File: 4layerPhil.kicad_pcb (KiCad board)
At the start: 4 copper layers, 71 x 54 mm, 55 parts, among them J1 USB_C_Receptacle_USB2.0_16P, J2 Conn_01x05_Pin, J3 Conn_01x04_Pin, J6 1140084168, SW1 SW_SPDT, SW2 BTN1, SW3 BTN2, SW4 BTN3, U2 USBLC6-2SC6, U3 STM32F103RCTx, U4 SPX3819M5-L-3-3, Y1 16MHz

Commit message: Added colours to schematic
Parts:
- removed H1, H2, H3, H4: MountingHole, MountingHole:MountingHole_2.2mm_M2
- added FID1: Fiducial, Fiducial:Fiducial_1mm_Mask2mm, F.Cu at (116.5, 58.0)
- added FID2: Fiducial, Fiducial:Fiducial_1mm_Mask2mm, F.Cu at (116.2, 104.0)
- added FID3: Fiducial, Fiducial:Fiducial_1mm_Mask2mm, F.Cu at (169.0, 103.8)
- added MH1: M3, MountingHole:MountingHole_3.2mm_M3_Pad_Via, F.Cu at (111.1, 58.0)
- added MH2: M3, MountingHole:MountingHole_3.2mm_M3_Pad_Via, F.Cu at (174.0, 57.9)
- added MH3: M3, MountingHole:MountingHole_3.2mm_M3_Pad_Via, F.Cu at (111.0, 104.0)
- added MH4: M3, MountingHole:MountingHole_3.2mm_M3_Pad_Via, F.Cu at (174.0, 104.0)
- C1, C20, C22: footprint Capacitor_SMD:C_0603_1608Metric -> Capacitor_SMD:C_0805_2012Metric
- moved U4 41.0 mm to (160.1, 79.8), turned to 180 degrees
- moved R8 40.4 mm to (170.5, 65.8), turned to 180 degrees
- moved C21 38.8 mm to (160.0, 77.2)
- moved R24 38.2 mm to (167.3, 74.2), turned to 180 degrees
- moved C22 36.5 mm to (157.0, 79.7), turned to 90 degrees
- moved C20 33.9 mm to (163.2, 79.8), turned to -90 degrees
- moved C19 31.0 mm to (166.6, 76.5), turned to -90 degrees
- moved R7 29.1 mm to (172.0, 78.0), turned to 180 degrees
- moved C18 28.8 mm to (168.1, 76.5), turned to -90 degrees
- moved U2 6.94 mm to (165.4, 71.8)
- moved R4 3.72 mm to (153.2, 73.6)
- moved R2 3.72 mm to (153.2, 77.6)
- moved R3 3.72 mm to (153.2, 75.6)
- moved D2 3.04 mm to (148.2, 77.8)
- moved D3 3.04 mm to (148.2, 75.6)
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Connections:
- net Net-(U4-BP) renamed /BP_REG
- U2 pad 1: /USB_D- -> /USB_D+
- U2 pad 3: /USB_D+ -> /USB_D-
- U2 pad 4: /D_USB+ -> /D_USB-
- U2 pad 6: /D_USB- -> /D_USB+
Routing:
- net +3V3: track 218.9 -> 180.5 mm, vias 21 -> 18
- net VBUSF: track 0.00 -> 10.7 mm
- net /USR_LED_RED: track 8.32 -> 0.00 mm
- net /USBCC1: track 0.00 -> 7.64 mm
- net /USR_LED_BLU: track 7.60 -> 0.00 mm
- net /USBCC2: track 0.00 -> 7.54 mm
- net /USB_D-: track 13.8 -> 20.9 mm
- net /USB_D+: track 13.8 -> 20.9 mm
- net VBUS: track 0.00 -> 7.01 mm, vias 0 -> 1
- net /USR_LED_GRN: track 6.87 -> 0.00 mm
- net GND: track 62.8 -> 56.2 mm, vias 27 -> 34
- net /D_USB+: track 2.25 -> 8.37 mm
- net /D_USB-: track 2.24 -> 7.34 mm
- net /USR_LED_GRN_K: track 4.43 -> 0.00 mm
- net /USR_LED_BLU_K: track 4.33 -> 0.00 mm
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- added copper zone on B.Cu, net GND
- removed copper zone on In1.Cu, net GND
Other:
- outline, holes or cut-outs redrawn
- copper layers 4 -> 2

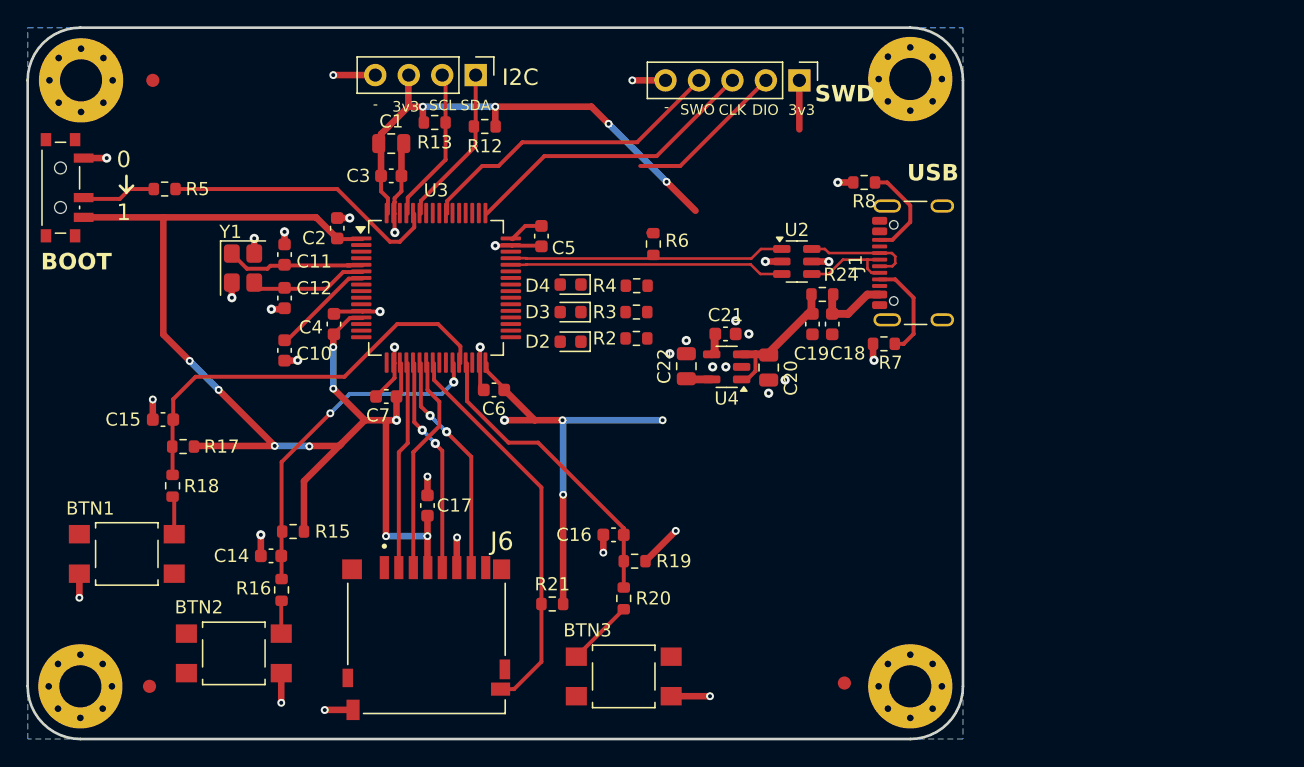
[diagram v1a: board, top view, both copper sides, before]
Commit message: New microSD card
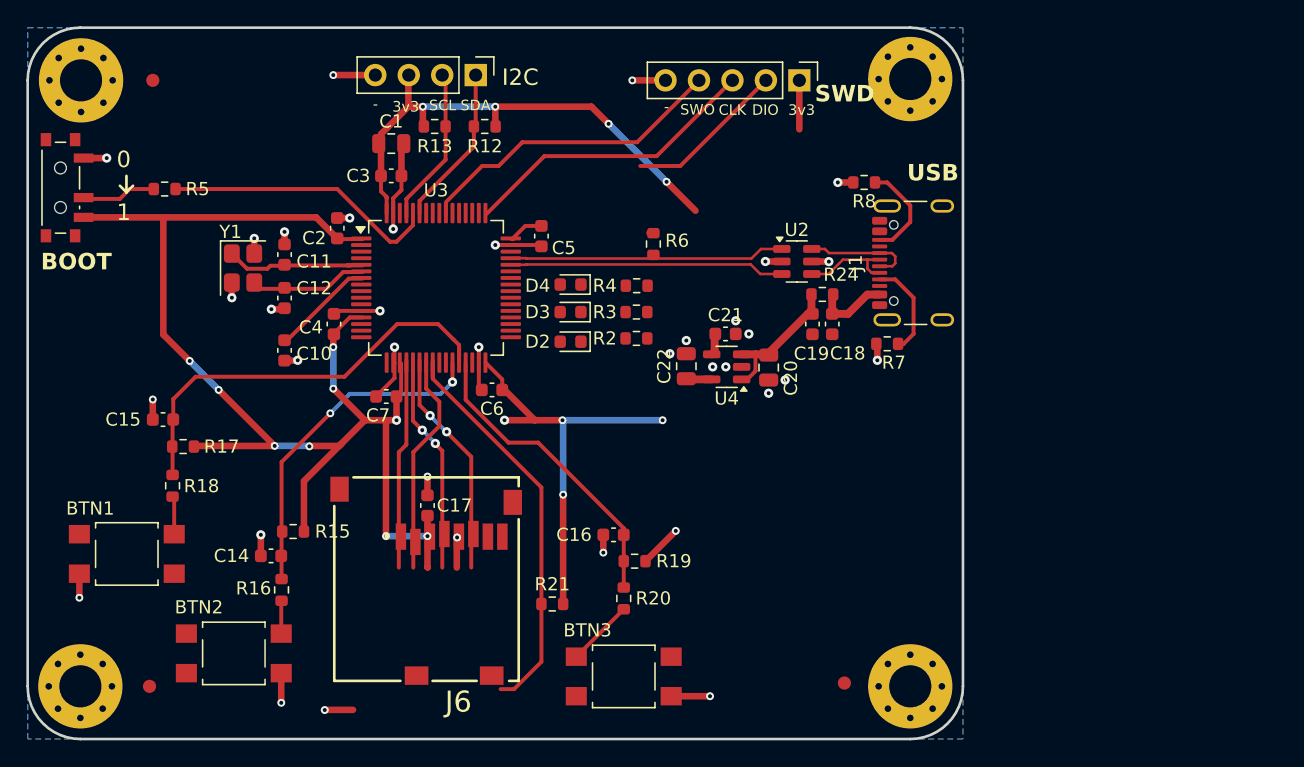
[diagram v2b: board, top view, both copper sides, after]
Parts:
- J6: footprint MicroSD_Socket:AMPHENOL_1140084168 -> MicroSD_Socket:GCT_MEM2061-01-188-00-A_REVA
- moved R13 0.30 mm to (137.9, 61.5)
- moved R7 0.25 mm to (172.2, 78.0)
- moved C6 0.15 mm to (142.2, 81.5)
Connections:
- net /USR_LED_BLU_K renamed /LED_BLU_K
- net /USR_LED_GRN renamed /LED_GRN
- net /USR_LED_GRN_K renamed /LED_GRN_K
- net /USR_LED_RED_K renamed /LED_RED_K
- net VBUS renamed +VBUS
- net VBUSF renamed +VBUSF
- D2 pad 2: /USR_LED_RED -> /LED_BLU
- D3 pad 2: /USR_LED_BLU -> /LED_BLU
- J1 pad A6: /D_USB+ -> /USB_D+
- J1 pad A7: /D_USB- -> /USB_D-
- J1 pad B6: /D_USB+ -> /USB_D+
- J1 pad B7: /D_USB- -> /USB_D-
- R6 pad 2: /USB_D+ -> /USB_D_ESD+
- U2 pad 1: /USB_D+ -> /USB_D_ESD+
- U2 pad 3: /USB_D- -> /USB_D_ESD-
- U2 pad 4: /D_USB- -> /USB_D-
- U2 pad 6: /D_USB+ -> /USB_D+
- U3 pad 40: /USR_LED_RED -> /LED_BLU
- U3 pad 41: /USR_LED_BLU -> /LED_BLU
- U3 pad 44: /USB_D- -> /USB_D_ESD-
- U3 pad 45: /USB_D+ -> /USB_D_ESD+
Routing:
- net /USB_D_ESD+: track 0.00 -> 20.9 mm
- net /USB_D_ESD-: track 0.00 -> 20.9 mm
- net /USB_D-: track 20.9 -> 7.34 mm
- net /USB_D+: track 20.9 -> 8.37 mm
- net /D_USB+: track 8.37 -> 0.00 mm
- net /D_USB-: track 7.34 -> 0.00 mm
- net SPI_SCK: track 16.4 -> 19.0 mm, vias 2 -> 3
- net GND: track 56.2 -> 53.6 mm, vias 34 -> 33
- net MICROSD_DETB: track 30.0 -> 31.4 mm
- net USR_BTN_2: track 31.9 -> 33.1 mm

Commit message: Managed to make the PCB ~5 mm smaller in both directions
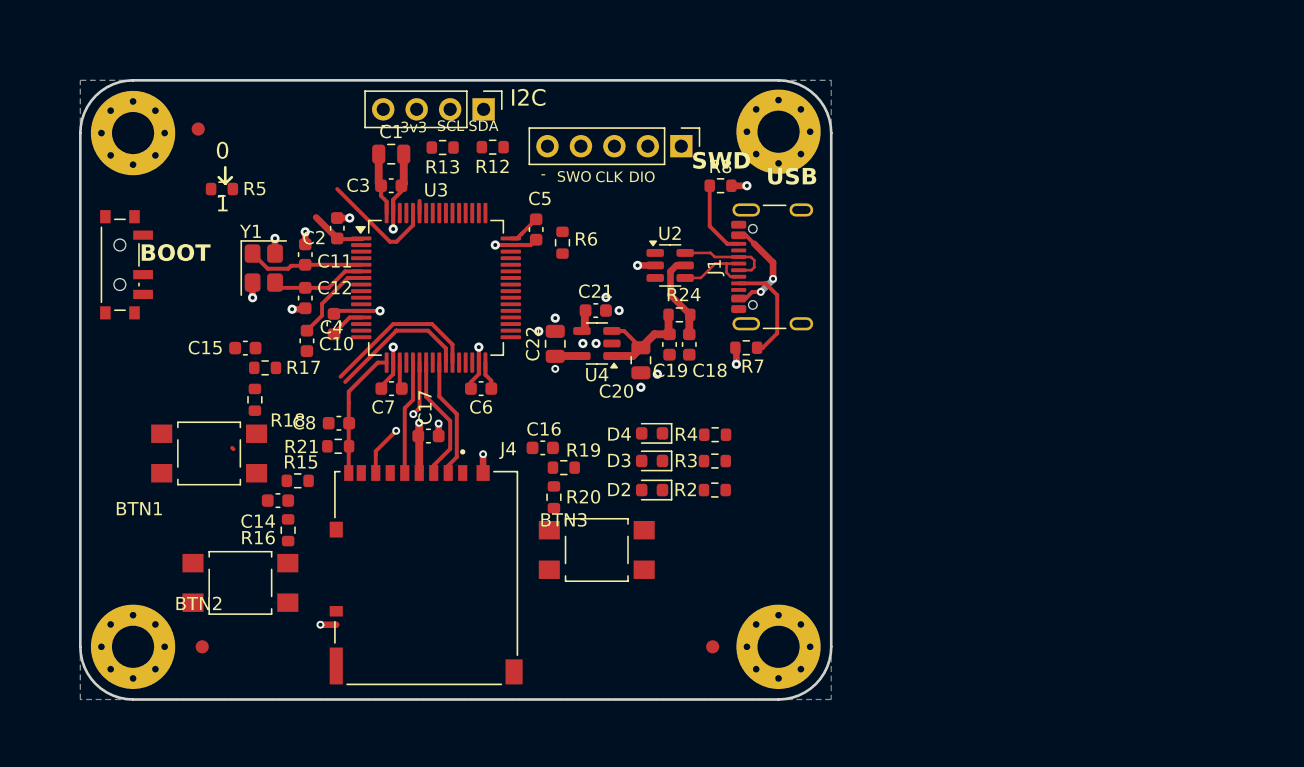
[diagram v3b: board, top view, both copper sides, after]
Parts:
- removed J6: 1140084168, MicroSD_Socket:GCT_MEM2061-01-188-00-A_REVA
- added C8: 100n, Capacitor_SMD:C_0603_1608Metric, F.Cu at (130.6, 84.0)
- added J4: DM3AT-SF-PEJM5, microSD_DM3AT:HRS_DM3AT-SF-PEJM5, F.Cu at (137.2, 95.8)
- R21: value 10k -> 56k
- moved R21 20.2 mm to (130.6, 85.8), turned to 180 degrees
- moved R2 13.0 mm to (159.2, 89.1)
- moved D3 12.9 mm to (154.4, 86.9)
- moved D4 12.9 mm to (154.4, 84.8)
- moved D2 12.8 mm to (154.4, 89.1)
- moved R4 12.8 mm to (159.2, 84.9)
- moved R3 12.8 mm to (159.2, 86.9)
- moved C18 11.0 mm to (157.2, 78.0)
- moved C19 11.0 mm to (155.7, 78.0)
- moved R24 11.0 mm to (156.5, 75.8)
- moved R8 10.9 mm to (159.6, 66.0), turned to 0 degrees
- moved MH2 10.8 mm to (164.0, 61.9)
- moved J1 10.7 mm to (164.7, 72.2)
- moved R7 10.7 mm to (161.6, 78.3)
- moved MH4 10.4 mm to (164.0, 101.0)
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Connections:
- C17 pad 1: GND -> +3V3
- C17 pad 2: +3V3 -> GND
- U3 pad 17: unconnected-(U3-PA3-Pad17) -> MICROSD_DETB
- U3 pad 20: SPI_NSS -> unconnected-(U3-PA4-Pad20)
- U3 pad 24: MICROSD_DETB -> unconnected-(U3-PC4-Pad24)
- U3 pad 25: unconnected-(U3-PC5-Pad25) -> SPI_NSS
- U3 pad 26: unconnected-(U3-PB0-Pad26) -> USR_BTN_1
- U3 pad 27: USR_BTN_1 -> USR_BTN_2
- U3 pad 28: USR_BTN_2 -> USR_BTN_3
- U3 pad 29: USR_BTN_3 -> unconnected-(U3-PB10-Pad29)
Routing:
- net +3V3: track 180.6 -> 24.2 mm, vias 18 -> 2
- net /SWO: track 23.9 -> 0.00 mm
- net USR_BTN_3: track 23.3 -> 0.00 mm
- net /SWCLK: track 22.8 -> 0.00 mm
- net MICROSD_DETB: track 31.4 -> 9.97 mm
- net USR_BTN_2: track 33.1 -> 12.2 mm
- net /USB_D_ESD+: track 20.9 -> 0.00 mm
- net /USB_D_ESD-: track 20.9 -> 0.00 mm
- net GND: track 53.6 -> 33.0 mm, vias 33 -> 24
- net USR_BTN_1: track 26.0 -> 10.9 mm, vias 2 -> 0
- net /SWDIO: track 12.2 -> 0.00 mm
- net /BOOT0: track 21.0 -> 8.85 mm
- net /I2C1_SCL: track 12.1 -> 0.00 mm
- net /I2C1_SDA: track 12.3 -> 1.17 mm
- net SPI_SCK: track 19.0 -> 8.64 mm, vias 3 -> 0
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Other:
- board size 71 x 54 mm -> 57 x 47 mm

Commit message: Finished signal routing and layout, started power routing
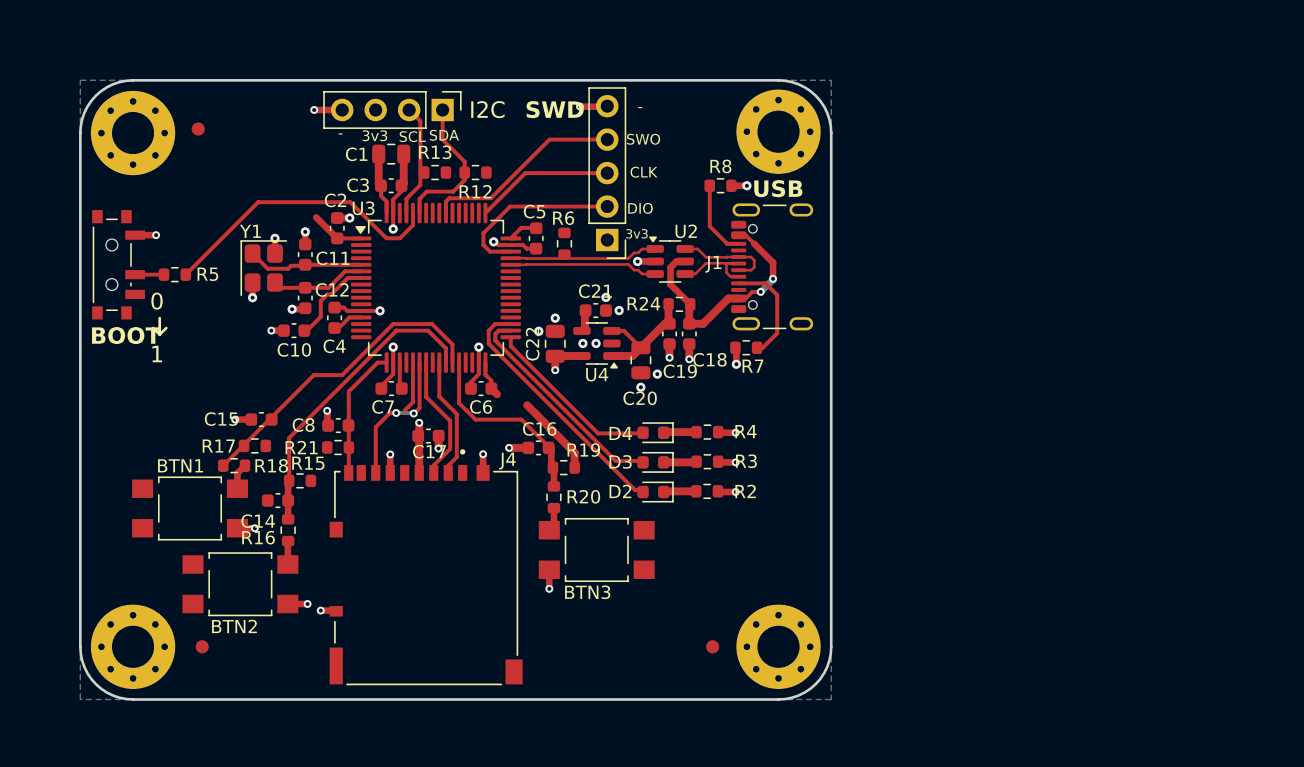
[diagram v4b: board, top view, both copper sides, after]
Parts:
- R2, R4: value 1k -> 1.5k
- R7, R8: value 5.1k -> 5k1
- moved J2 9.07 mm to (151.0, 70.1), turned to 180 degrees
- moved R5 7.42 mm to (118.2, 72.8)
- moved R17 5.98 mm to (124.2, 85.8)
- moved C15 5.56 mm to (124.8, 83.8)
- moved R18 5.24 mm to (122.7, 87.2), turned to 0 degrees
- moved SW3 4.42 mm to (119.3, 90.5)
- moved J3 3.11 mm to (138.5, 60.2)
- moved R12 2.33 mm to (141.0, 65.0)
- moved R13 1.99 mm to (137.9, 65.0), turned to 180 degrees
- moved C10 1.25 mm to (127.2, 77.0), turned to 180 degrees
- moved C18 0.80 mm to (157.2, 77.2)
- moved C19 0.80 mm to (155.7, 77.2)
- moved R24 0.80 mm to (156.5, 75.0)
- moved C5 0.67 mm to (145.6, 70.0)
- moved R4 0.62 mm to (158.6, 84.7)
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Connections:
- D2 pad 2: /LED_BLU -> /LED_RED
- U3 pad 33: unconnected-(U3-PB12-Pad33) -> /LED_GRN
- U3 pad 34: unconnected-(U3-PB13-Pad34) -> /LED_BLU
- U3 pad 35: unconnected-(U3-PB14-Pad35) -> /LED_RED
- U3 pad 40: /LED_BLU -> unconnected-(U3-PC9-Pad40)
- U3 pad 41: /LED_BLU -> unconnected-(U3-PA8-Pad41)
- U3 pad 42: /LED_GRN -> unconnected-(U3-PA9-Pad42)
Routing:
- net GND: track 33.0 -> 54.4 mm, vias 24 -> 40
- net /LED_RED: track 0.00 -> 19.1 mm
- net /LED_BLU: track 0.00 -> 16.7 mm
- net USR_BTN_3: track 0.00 -> 14.7 mm
- net /SWO: track 0.00 -> 14.6 mm
- net /LED_GRN: track 0.00 -> 13.4 mm
- net /BOOT0: track 8.85 -> 22.0 mm
- net /SWDIO: track 0.00 -> 12.9 mm
- net USR_BTN_1: track 10.9 -> 23.2 mm
- net USR_BTN_2: track 12.2 -> 23.9 mm
- net /USB_D_ESD-: track 0.00 -> 11.3 mm
- net /USB_D_ESD+: track 0.00 -> 11.3 mm
- net /SWCLK: track 0.00 -> 10.0 mm
- net /I2C1_SDA: track 1.17 -> 11.1 mm
- net /I2C1_SCL: track 0.00 -> 8.62 mm
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
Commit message: Finished pcb routing and layout but preparing to change the regulator to a buck converter for better thermals
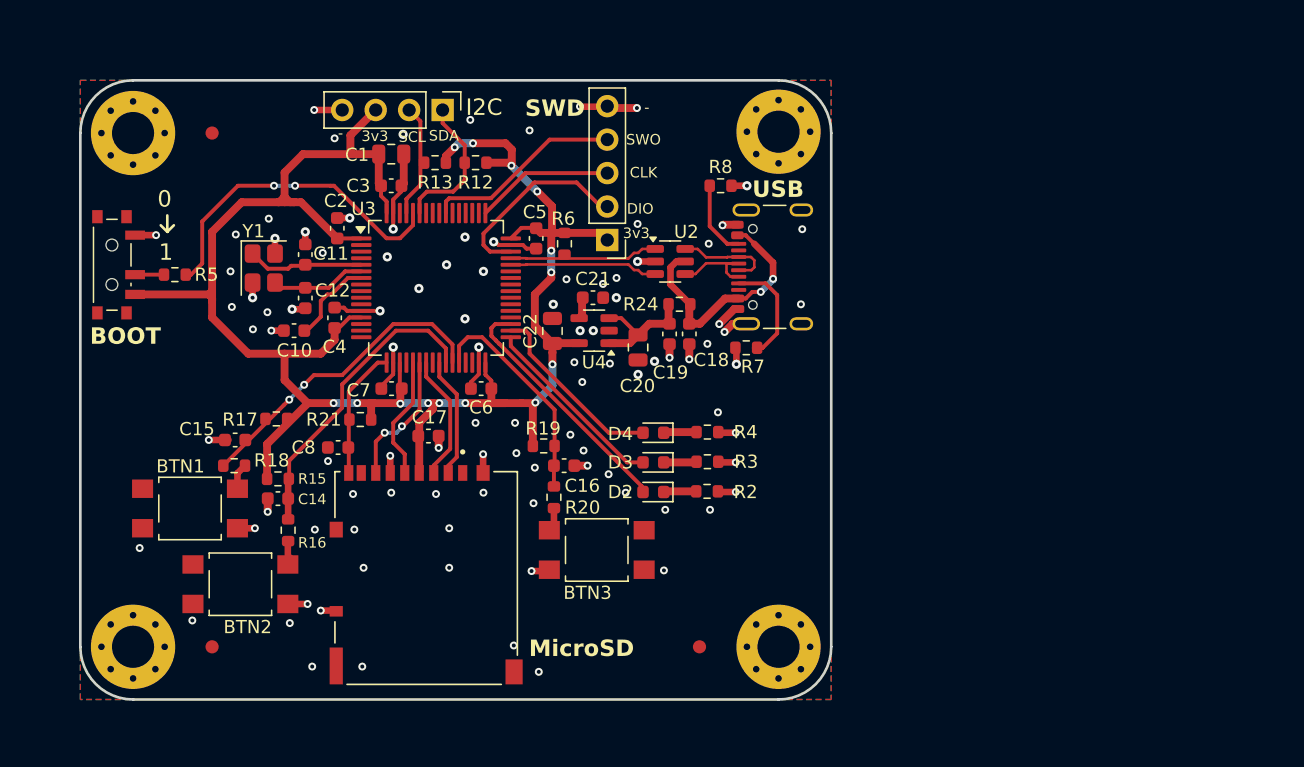
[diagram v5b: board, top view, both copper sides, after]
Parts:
- removed FID1, FID2: Fiducial, Fiducial:Fiducial_1mm_Mask2mm
- added ?: , , F.Cu at (158.0, 101.0)
- added ?: , , F.Cu at (121.0, 62.0)
- moved FID3 38.0 mm to (121.0, 101.0)
- moved R21 2.71 mm to (132.2, 83.8), turned to 0 degrees
- moved R17 2.62 mm to (125.9, 83.7)
- moved C15 2.53 mm to (122.8, 85.3)
- moved C16 2.37 mm to (147.7, 87.2), turned to 0 degrees
- moved R19 2.25 mm to (146.2, 85.8), turned to 180 degrees
- moved R15 1.68 mm to (126.0, 88.2), turned to 180 degrees
- moved C8 1.67 mm to (130.6, 85.9)
- moved C20 1.00 mm to (153.3, 78.3)
- moved C21 1.00 mm to (149.9, 74.5)
- moved C22 1.00 mm to (146.8, 77.0)
- moved U4 1.00 mm to (150.0, 77.0)
- moved R12 0.75 mm to (141.0, 64.2)
- moved R13 0.75 mm to (137.9, 64.2)
- moved C14 0.15 mm to (126.0, 89.8)
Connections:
- U3 pad 33: /LED_GRN -> /LED_BLU
- U3 pad 34: /LED_BLU -> /LED_GRN
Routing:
- net +3V3: track 31.9 -> 149.4 mm, vias 2 -> 14
- net GND: track 54.4 -> 61.4 mm, vias 40 -> 100
- net SPI_SCK: track 3.89 -> 9.36 mm
- net /BOOT0: track 22.0 -> 24.9 mm, vias 0 -> 2
- net /LED_BLU: track 16.7 -> 14.4 mm
- net USR_BTN_3: track 14.7 -> 16.9 mm
- net /SWDIO: track 12.9 -> 14.4 mm
- net /LED_GRN: track 13.4 -> 14.1 mm
- net SPI_MISO: track 10.9 -> 10.3 mm
- net USR_BTN_2: vias 0 -> 2
- added copper zone on F.Cu, net GND
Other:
- board text added: "MicroSD"

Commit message: Removed LDO in favour of Buck converter, assigned footprints, ready to layout on the PCB
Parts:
- removed ? (x2): , 
- removed C18, C19, C21: 470n, Capacitor_SMD:C_0603_1608Metric
- removed C20, C22: 10u, Capacitor_SMD:C_0805_2012Metric
- removed R24: 0, Resistor_SMD:R_0603_1608Metric
- added C13: 22u, Capacitor_SMD:C_0805_2012Metric, F.Cu at (181.0, 74.0)
- added C9: 4u7, Capacitor_SMD:C_0805_2012Metric, F.Cu at (193.2, 74.0)
- added FID1: Fiducial, Fiducial:Fiducial_1mm_Mask2mm, F.Cu at (121.0, 62.0)
- added FID2: Fiducial, Fiducial:Fiducial_1mm_Mask2mm, F.Cu at (158.0, 101.0)
- added L1: 2u2, Inductor_SMD:L_0805_2012Metric, F.Cu at (186.6, 77.8)
- added R1: 90k, Resistor_SMD:R_0603_1608Metric, F.Cu at (191.5, 78.5)
- added R9: 20k, Resistor_SMD:R_0603_1608Metric, F.Cu at (195.1, 82.3)
- U4: value SPX3819M5-L-3-3 -> TLV62569DBV
- moved U4 38.9 mm to (188.8, 73.9)
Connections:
- U4 pad 1: +VBUSF -> +VBUS
- U4 pad 3: +VBUSF -> /BUCK_SW
- U4 pad 4: /BP_REG -> +VBUS
- U4 pad 5: +3V3 -> /BUCK_FB
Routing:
- net +VBUSF: track 9.86 -> 0.00 mm
- net +VBUS: track 18.7 -> 11.6 mm
- net +3V3: track 149.4 -> 144.7 mm
- net /BP_REG: track 1.66 -> 0.00 mm
- net GND: track 61.4 -> 60.3 mm, vias 100 -> 85
- removed copper zone on F.Cu, net GND

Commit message: Added LM3671MF buck converter
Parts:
- removed R1: 90k, Resistor_SMD:R_0603_1608Metric
- removed R9: 20k, Resistor_SMD:R_0603_1608Metric
- removed U4: TLV62569DBV, Package_TO_SOT_SMD:SOT-23-5
- added U1: LM3671MF-3.3, Buck_LM3671:SOT95P280X145-5N, F.Cu at (187.7, 73.3)
- C13: value 22u -> 10u
- moved C13 14.3 mm to (195.2, 73.3)
- moved C9 9.78 mm to (183.5, 73.2), turned to -90 degrees
- moved L1 7.74 mm to (192.0, 72.2)

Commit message: Added and laid out new power supply section with new buck converter
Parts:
- added D1: PWR LED, LED_SMD:LED_0603_1608Metric, F.Cu at (150.0, 79.5)
- added R1: 1.5k, Resistor_SMD:R_0603_1608Metric, F.Cu at (154.0, 79.5)
- moved C13 46.3 mm to (149.1, 75.6)
- moved L1 40.9 mm to (151.2, 75.7), turned to 90 degrees
- moved U1 33.4 mm to (154.4, 75.8), turned to 180 degrees
- moved C9 26.0 mm to (157.8, 77.2)
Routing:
- net +3V3: track 144.7 -> 155.9 mm
- net +VBUS: track 11.6 -> 20.7 mm
- net /USR_BTN_3R: track 1.82 -> 9.02 mm
- net /USR_BTN_2R: track 1.99 -> 9.19 mm
- net /USR_BTN_1R: track 1.72 -> 8.92 mm
- net /LED_PWR_K: track 0.00 -> 2.39 mm
- net /BUCK_SW: track 0.00 -> 2.02 mm
- net GND: track 60.3 -> 61.1 mm, vias 85 -> 95
- added copper zone on F.Cu, net GND
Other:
- rule pad_to_mask_clearance: 0.1 -> 0.025
